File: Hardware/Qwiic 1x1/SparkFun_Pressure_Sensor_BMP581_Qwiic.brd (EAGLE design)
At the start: 25.4 x 25.4 mm, 48 parts, among them J1 QWIIC_RIGHT_ANGLE, J2 QWIIC_RIGHT_ANGLE, U1 BMP581

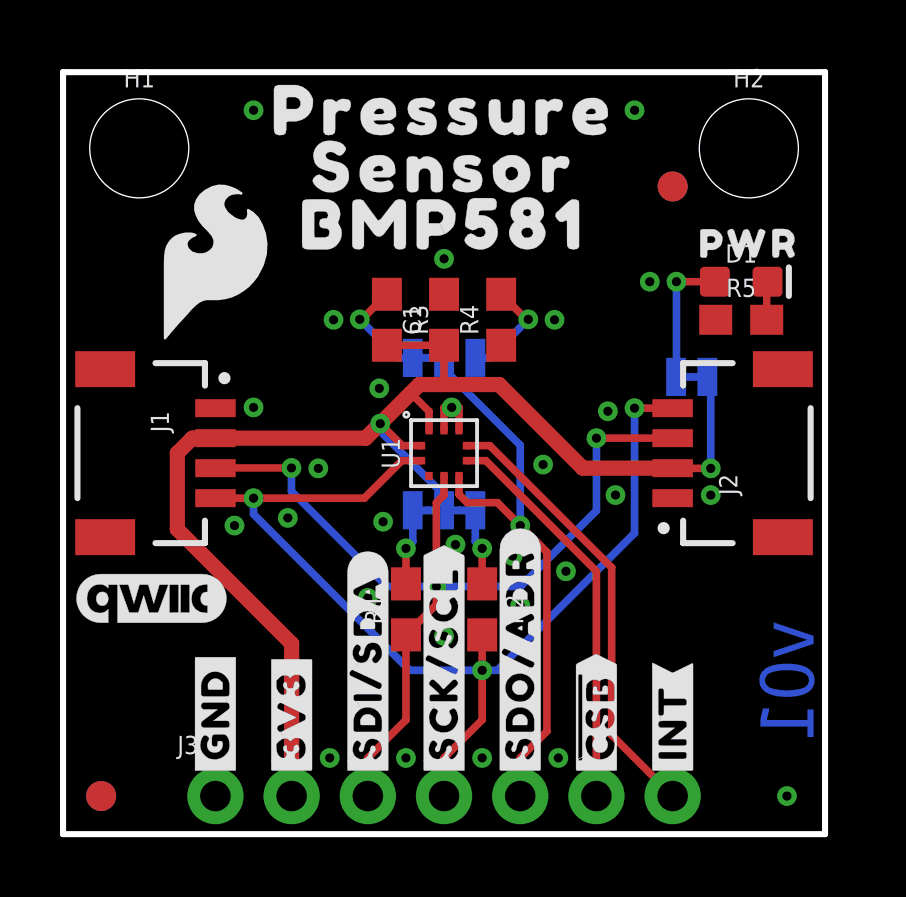
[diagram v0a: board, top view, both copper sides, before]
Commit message: Design review updates
Rename files
Change to v10 (accelerating to reds)
Fix sensor name in schematic
Add note to schematic about max wire diameter in Micro PTH connectors
Update VDD range
Fix acid trap in Micro
Move PWR LED to give space
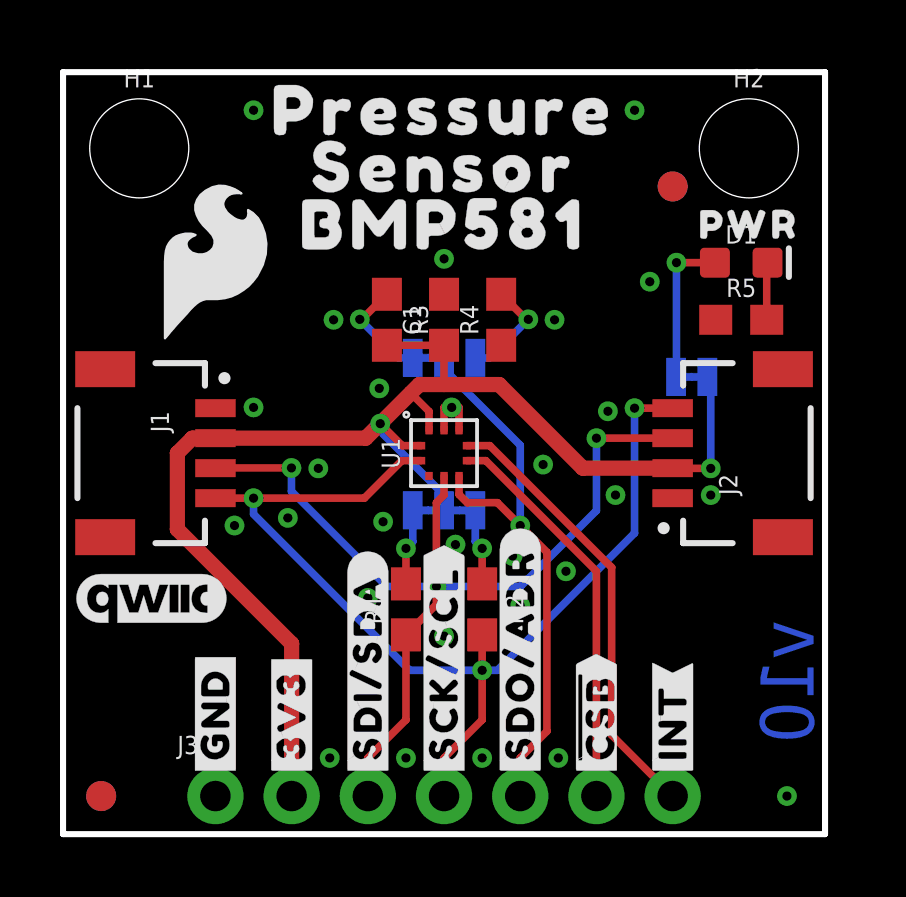
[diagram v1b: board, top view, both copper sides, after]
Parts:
- moved D1 0.64 mm to (22.6, 19.1)
- moved U$16 0.64 mm to (22.9, 20.3)
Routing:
- net N$5: track 4.46 -> 5.10 mm
- net N$6: track 1.28 -> 1.92 mm
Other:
- board text added: "v10"
- board text removed: "v01"
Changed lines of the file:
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@@
 <drawing>
 <settings>
-<setting alwaysvectorfont="yes"/>
+<setting alwaysvectorfont="no"/>
 <setting verticaltext="up"/>
 </settings>
@@
 <rectangle x1="13.462" y1="13.335" x2="13.589" y2="13.589" layer="41"/>
 <rectangle x1="12.827" y1="13.335" x2="12.954" y2="13.589" layer="41"/>
-<text x="24.13" y="5.08" size="1.778" layer="16" font="vector" ratio="15" rot="SMR270" align="center">v01</text>
+<text x="24.13" y="5.08" size="1.778" layer="16" font="vector" ratio="15" rot="SMR270" align="center">v10</text>
 <text x="16.51" y="-21.59" size="1.778" layer="51" font="vector">Dryw Wade</text>
 <dimension x1="0" y1="0" x2="5.08" y2="0" x3="2.54" y3="-3.81" textsize="1.778" textratio="15" layer="47" unit="inch"/>
@@
 <attribute name="VALUE" x="13.462" y="17.145" size="0.6096" layer="27" font="vector" ratio="20" rot="R90" align="top-center"/>
 </element>
-<element name="D1" library="SparkFun-LED" package="LED-0603" value="RED" x="22.606" y="18.415" smashed="yes">
-<attribute name="NAME" x="22.606" y="19.05" size="0.6096" layer="25" font="vector" ratio="20" align="bottom-center"/>
-<attribute name="PROD_ID" value="DIO-00819" x="41.656" y="-9.525" size="1.778" layer="27" display="off"/>
-<attribute name="VALUE" x="22.606" y="17.78" size="0.6096" layer="27" font="vector" ratio="20" align="top-center"/>
+<element name="D1" library="SparkFun-LED" package="LED-0603" value="RED" x="22.606" y="19.05" smashed="yes">
+<attribute name="NAME" x="22.606" y="19.685" size="0.6096" layer="25" font="vector" ratio="20" align="bottom-center"/>
+<attribute name="PROD_ID" value="DIO-00819" x="41.656" y="-8.89" size="1.778" layer="27" display="off"/>
+<attribute name="VALUE" x="22.606" y="18.415" size="0.6096" layer="27" font="vector" ratio="20" align="top-center"/>
 </element>
 <element name="FD1" library="SparkFun-Aesthetics" package="FIDUCIAL-1X2" value="FIDUCIAL1X2" x="20.32" y="21.59" smashed="yes" rot="MR0"/>
@@
 <element name="U$12" library="output" package="#0X46#0" value="" x="14.097" y="15.875" smashed="yes" rot="MR0"/>
 <element name="U$15" library="output" package="#0X47#0" value="" x="11.303" y="15.875" smashed="yes" rot="MR0"/>
-<element name="U$16" library="output" package="PWR0" value="" x="22.86" y="19.685" smashed="yes"/>
+<element name="U$16" library="output" package="PWR0" value="" x="22.86" y="20.32" smashed="yes"/>
 </elements>
 <signals>
@@
 <contactref element="JP3" pad="1"/>
 <contactref element="D1" pad="A"/>
-<wire x1="21.729" y1="18.415" x2="20.447" y2="18.415" width="0.254" layer="1"/>
-<via x="20.447" y="18.415" extent="1-16" drill="0.3048"/>
-<wire x1="20.447" y1="18.415" x2="20.447" y2="15.2527" width="0.254" layer="16"/>
+<wire x1="21.729" y1="19.05" x2="20.447" y2="19.05" width="0.254" layer="1"/>
+<via x="20.447" y="19.05" extent="1-16" drill="0.3048"/>
+<wire x1="20.447" y1="19.05" x2="20.447" y2="15.2527" width="0.254" layer="16"/>
 <wire x1="20.447" y1="15.2527" x2="20.4343" y2="15.24" width="0.254" layer="16"/>
 </signal>
@@
 <contactref element="D1" pad="C"/>
 <contactref element="R5" pad="2"/>
-<wire x1="23.456" y1="17.145" x2="23.456" y2="18.388" width="0.254" layer="1"/>
-<wire x1="23.456" y1="18.388" x2="23.483" y2="18.415" width="0.254" layer="1"/>
+<wire x1="23.456" y1="17.145" x2="23.456" y2="19.023" width="0.254" layer="1"/>
+<wire x1="23.456" y1="19.023" x2="23.483" y2="19.05" width="0.254" layer="1"/>
 </signal>
 </signals>
